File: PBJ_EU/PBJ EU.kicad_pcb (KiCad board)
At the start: 2 copper layers, 111.4 x 128.5 mm, 79 parts, among them J1 Molex_47257-spankulator-rescue, J2 Molex_47257-spankulator-rescue, J3 Molex_47257-spankulator-rescue, J4 Molex_47257-spankulator-rescue, J7 Conn_02x08_Odd_Even, J9 Conn_02x08_Odd_Even, SW1 SW_SPDT, SW2 SW_SPDT, U1 TL072, U2 TL072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

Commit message: ver 3.0
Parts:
- removed C10, C11, C8, C9: .1uF, Capacitor_THT:C_Rect_L7.0mm_W2.0mm_P5.00mm
- removed R25, R26: 91K, Resistor_THT:R_Axial_DIN0207_L6.3mm_D2.5mm_P10.16mm_Horizontal
- removed R28, R29, R5: 200K, Resistor_THT:R_Axial_DIN0207_L6.3mm_D2.5mm_P10.16mm_Horizontal
- removed U3, U4: TL072, Package_DIP:DIP-8_W7.62mm
- added D12: 1N4733A, Diode_THT:D_DO-41_SOD81_P10.16mm_Horizontal, F.Cu at (75.6, 131.0)
- added D14: 1N4733A, Diode_THT:D_DO-41_SOD81_P10.16mm_Horizontal, F.Cu at (104.5, 131.0)
- added D15: 1N4733A, Diode_THT:D_DO-41_SOD81_P10.16mm_Horizontal, F.Cu at (101.7, 131.0)
- added D16: 1N4733A, Diode_THT:D_DO-41_SOD81_P10.16mm_Horizontal, F.Cu at (143.9, 132.7)
- added D17: 1N4733A, Diode_THT:D_DO-41_SOD81_P10.16mm_Horizontal, F.Cu at (147.3, 129.1)
- added D3: 1N4733A, Diode_THT:D_DO-41_SOD81_P10.16mm_Horizontal, F.Cu at (49.7, 132.6)
- added D6: 1N4733A, Diode_THT:D_DO-41_SOD81_P10.16mm_Horizontal, F.Cu at (49.7, 129.3)
- added D9: 1N4733A, Diode_THT:D_DO-41_SOD81_P10.16mm_Horizontal, F.Cu at (78.5, 131.0)
- added R3: 470, Resistor_THT:R_Axial_DIN0207_L6.3mm_D2.5mm_P10.16mm_Horizontal, F.Cu at (104.7, 135.9)
- C4, C5, C6, C7, R10, R11, R16, R17, R34, R35, R40, R41, R43, U1, U2, U7: moved to B.Cu
- D1, D2, D7, D8: value LED -> RED LED
- D10, D11, D4, D5: value LED -> BLUE LED
- D13: value LED -> GREEN LED
- J9: value Conn_02x08_Odd_Even -> Conn_02x08_Odd_Even_Female
- R1, R2: value 91K -> 470
- R13, R14, R22, R23, R37, R38, R47, R48: value 100 -> 1K
- R4: value 200K -> 470
- moved R4 95.9 mm to (143.9, 135.9), turned to 180 degrees
- moved C7 66.5 mm to (126.4, 99.5), turned to 180 degrees
- moved C5 50.3 mm to (71.0, 99.6), turned to 180 degrees
- moved C6 45.9 mm to (126.5, 113.2)
- moved U2 42.8 mm to (120.2, 110.2)
- moved R40 36.0 mm to (74.3, 105.2), turned to 0 degrees
- moved R41 35.4 mm to (130.1, 105.2), turned to 0 degrees
- moved R16 28.0 mm to (62.2, 107.6), turned to 180 degrees
- moved R17 27.8 mm to (118.0, 107.7), turned to 180 degrees
- moved C4 27.1 mm to (70.8, 113.2)
- moved R34 24.1 mm to (84.5, 102.0), turned to 180 degrees
- moved R35 23.7 mm to (140.2, 102.1), turned to 180 degrees
- moved R10 22.8 mm to (52.1, 104.5), turned to 0 degrees
- moved R11 22.4 mm to (107.8, 104.6), turned to 0 degrees
- moved U1 20.7 mm to (64.5, 110.2)
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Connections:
- D1 pad 1: GND -> Net-(D1-Pad1)
- D1 pad 2: Net-(D1-Pad2) -> GND
- D2 pad 1: GND -> Net-(D2-Pad1)
- D2 pad 2: Net-(D2-Pad2) -> GND
- D7 pad 1: GND -> Net-(D7-Pad1)
- D7 pad 2: Net-(D7-Pad2) -> GND
- D8 pad 1: GND -> Net-(D8-Pad1)
- D8 pad 2: Net-(D8-Pad2) -> GND
- R1 pad 1: Net-(R1-Pad1) -> Tip1
- R1 pad 2: GND -> Net-(D3-Pad2)
- R10 pad 1: Tip1 -> Net-(D3-Pad2)
- R11 pad 1: Tip3 -> Net-(D14-Pad2)
- R13 pad 2: Net-(D1-Pad2) -> Net-(D1-Pad1)
- R14 pad 2: Net-(D2-Pad2) -> Net-(D2-Pad1)
- R16 pad 2: Net-(R16-Pad2) -> Net-(R13-Pad1)
- R17 pad 2: Net-(R17-Pad2) -> Net-(R14-Pad1)
- R2 pad 1: Net-(R2-Pad1) -> Tip2
- R2 pad 2: GND -> Net-(D9-Pad2)
- R22 pad 1: Net-(R16-Pad2) -> Net-(R13-Pad1)
- R23 pad 1: Net-(R17-Pad2) -> Net-(R14-Pad1)
- R31 pad 1: +12V -> Net-(D7-Pad1)
- R31 pad 2: Net-(D7-Pad2) -> -12V
- R32 pad 1: +12V -> Net-(D8-Pad1)
- R32 pad 2: Net-(D8-Pad2) -> -12V
- R34 pad 1: Tip2 -> Net-(D9-Pad2)
- R35 pad 1: Tip4 -> Net-(D16-Pad2)
- R37 pad 1: Net-(R28-Pad2) -> Net-(R37-Pad1)
- R37 pad 2: Net-(D7-Pad2) -> Net-(D7-Pad1)
- R38 pad 1: Net-(R29-Pad2) -> Net-(R38-Pad1)
- R38 pad 2: Net-(D8-Pad2) -> Net-(D8-Pad1)
- R4 pad 1: Net-(R1-Pad1) -> Tip4
- R4 pad 2: Net-(R13-Pad1) -> Net-(D16-Pad2)
- R40 pad 2: Net-(R40-Pad2) -> Net-(R37-Pad1)
- R41 pad 2: Net-(R41-Pad2) -> Net-(R38-Pad1)
- R47 pad 1: Net-(R40-Pad2) -> Net-(R37-Pad1)
- R48 pad 1: Net-(R41-Pad2) -> Net-(R38-Pad1)
- R7 pad 1: +12V -> Net-(D1-Pad1)
- R7 pad 2: Net-(D1-Pad2) -> -12V
- R8 pad 1: +12V -> Net-(D2-Pad1)
- R8 pad 2: Net-(D2-Pad2) -> -12V
- U1 pad 2: Net-(R1-Pad1) -> Net-(R10-Pad2)
- U1 pad 3: Tip1 -> GND
- U1 pad 6: Net-(R10-Pad2) -> Net-(R34-Pad2)
- U1 pad 7: Net-(R16-Pad2) -> Net-(R37-Pad1)
- U2 pad 1: Net-(R28-Pad2) -> Net-(R14-Pad1)
- U2 pad 2: Net-(R25-Pad1) -> Net-(R11-Pad2)
- U2 pad 3: Tip2 -> GND
- U2 pad 6: Net-(R34-Pad2) -> Net-(R35-Pad2)
- U2 pad 7: Net-(R40-Pad2) -> Net-(R38-Pad1)
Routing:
- net Net-(R38-Pad1): track 0.00 -> 75.9 mm, vias 0 -> 1
- net Net-(R37-Pad1): track 0.00 -> 63.3 mm
- net -12V: track 164.0 -> 222.3 mm, vias 6 -> 4
- net Net-(D3-Pad2): track 0.00 -> 45.8 mm, vias 0 -> 1
- net Net-(D16-Pad2): track 0.00 -> 44.3 mm, vias 0 -> 1
- net Net-(R13-Pad1): track 17.7 -> 61.9 mm
- net Net-(D9-Pad2): track 0.00 -> 43.5 mm, vias 0 -> 1
- net Net-(R14-Pad1): track 27.2 -> 70.2 mm, vias 0 -> 1
- net Net-(D14-Pad2): track 0.00 -> 38.6 mm
- net Net-(R29-Pad2): track 30.6 -> 0.00 mm, vias 2 -> 0
- net Net-(D2-Pad1): track 0.00 -> 26.4 mm, vias 0 -> 1
- net Net-(D1-Pad2): track 25.9 -> 0.00 mm
- net Net-(D2-Pad2): track 25.9 -> 0.00 mm, vias 1 -> 0
- net Net-(D7-Pad2): track 24.2 -> 0.00 mm
- net Tip3: track 79.4 -> 55.3 mm, vias 3 -> 1
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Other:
- board text added: "v3.0"
- board text removed: "v2.0"

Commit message: Fixed rescue libs
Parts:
- removed D12, D14, D15, D16, D17, D3, D6, D9: 1N4733A, Diode_THT:D_DO-41_SOD81_P10.16mm_Horizontal
- removed R1, R2, R3, R4: 470, Resistor_THT:R_Axial_DIN0207_L6.3mm_D2.5mm_P10.16mm_Horizontal
- added GR1: small_logo, panel:small_face, F.Cu at (128.6, 132.1)
- added J10: Conn_02x05_Odd_Even, Connector_PinHeader_2.54mm:PinHeader_2x05_P2.54mm_Vertical, F.Cu at (142.3, 133.8)
- added SW5: SW_DPST, sputterizer:S202031MS02Q, F.Cu at (67.0, 128.5)
- C1, C2, R13, R14, R37, R38: moved to B.Cu
- J7: value Conn_02x08_Odd_Even -> Conn_02x05_Odd_Even; footprint Connector_PinHeader_2.54mm:PinHeader_2x08_P2.54mm_Vertical -> Connector_PinHeader_2.54mm:PinHeader_2x05_P2.54mm_Vertical
- R10, R11, R34, R35: value 100K -> 1.00M
- R16, R17, R40, R41: value 330K -> 3.32M
- R19, R20, R31, R32, R44, R45, R7, R8: value 20K -> 10K; moved to B.Cu
- R22, R23, R47, R48: value 1K -> 2.2K; moved to B.Cu
- moved R43 105.7 mm to (42.9, 118.0), turned to 90 degrees
- moved D13 105.7 mm to (42.9, 123.0), turned to 0 degrees
- moved C2 46.8 mm to (102.5, 86.8)
- moved U7 46.8 mm to (92.9, 86.8)
- moved C1 46.8 mm to (83.7, 87.0)
- moved R14 41.7 mm to (117.8, 110.7), turned to 180 degrees
- moved R38 40.4 mm to (130.1, 107.7), turned to 0 degrees
- moved R13 33.5 mm to (62.2, 110.7), turned to 180 degrees
- moved R47 32.3 mm to (74.6, 110.8), turned to 0 degrees
- moved R48 31.7 mm to (130.1, 110.8), turned to 0 degrees
- moved R7 30.9 mm to (52.1, 113.9), turned to 0 degrees
- moved R37 30.2 mm to (74.6, 107.7), turned to 0 degrees
- moved R44 27.8 mm to (76.8, 117.1), turned to 0 degrees
- moved R45 27.1 mm to (132.4, 116.9), turned to 0 degrees
- moved R32 24.6 mm to (140.3, 113.9)
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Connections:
- J7 pad 1: -12V -> Net-(J7-Pad1)
- J7 pad 10: +12V -> Net-(J7-Pad10)
- J7 pad 2: -12V -> Net-(J7-Pad1)
- J7 pad 9: +12V -> Net-(J7-Pad10)
- R10 pad 1: Net-(D3-Pad2) -> Tip1
- R11 pad 1: Net-(D14-Pad2) -> Tip3
- R34 pad 1: Net-(D9-Pad2) -> Tip2
- R35 pad 1: Net-(D16-Pad2) -> Tip4
- SW1 pad 1: Net-(SW1-Pad1) -> Tip1
- SW1 pad 3: Tip1 -> Net-(SW1-Pad3)
- SW2 pad 1: Net-(SW2-Pad1) -> Tip3
- SW2 pad 3: Tip3 -> Net-(SW2-Pad3)
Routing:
- net +5V: track 49.5 -> 142.3 mm
- net Net-(R38-Pad1): track 75.9 -> 18.6 mm, vias 1 -> 0
- net -12V: track 222.3 -> 169.3 mm, vias 4 -> 7
- net Net-(R14-Pad1): track 70.2 -> 24.3 mm, vias 1 -> 0
- net Net-(D3-Pad2): track 45.8 -> 0.00 mm, vias 1 -> 0
- net Net-(R37-Pad1): track 63.3 -> 18.4 mm
- net Net-(D16-Pad2): track 44.3 -> 0.00 mm, vias 1 -> 0
- net Net-(D9-Pad2): track 43.5 -> 0.00 mm, vias 1 -> 0
- net Net-(D14-Pad2): track 38.6 -> 0.00 mm
- net Net-(R13-Pad1): track 61.9 -> 24.3 mm
- net Net-(D11-Pad2): track 7.01 -> 41.0 mm
- net Net-(D10-Pad2): track 7.51 -> 40.0 mm
- net Net-(J7-Pad10): track 0.00 -> 31.7 mm
- net Tip3: track 55.3 -> 86.9 mm, vias 1 -> 4
- net Net-(J7-Pad1): track 0.00 -> 30.7 mm
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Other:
- board text added: "EU Power Out"
- board text added: "Mult 1&2"
- board text added: "Mult 3&4"
- board text added: "ON"
- board text added: "v4.0"
- board text removed: "v3.0"

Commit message: Updates to ver 4.7.
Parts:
- added R1: 750K, Resistor_THT:R_Axial_DIN0207_L6.3mm_D2.5mm_P10.16mm_Horizontal, B.Cu at (62.2, 98.0)
- added R2: 750K, Resistor_THT:R_Axial_DIN0207_L6.3mm_D2.5mm_P10.16mm_Horizontal, B.Cu at (117.9, 98.0)
- added R3: 750K, Resistor_THT:R_Axial_DIN0207_L6.3mm_D2.5mm_P10.16mm_Horizontal, B.Cu at (62.2, 101.3)
- added R4: 750K, Resistor_THT:R_Axial_DIN0207_L6.3mm_D2.5mm_P10.16mm_Horizontal, B.Cu at (117.8, 101.3)
- J1, J2, J3, J4: value Molex_47257-spankulator-rescue -> Molex_47257
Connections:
- U1 pad 3: GND -> Net-(R1-Pad1)
- U1 pad 5: GND -> Net-(R3-Pad1)
- U2 pad 3: GND -> Net-(R2-Pad1)
- U2 pad 5: GND -> Net-(R4-Pad1)
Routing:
- net Net-(R4-Pad1): track 0.00 -> 10.6 mm
- net Net-(R3-Pad1): track 0.00 -> 10.4 mm
- net Net-(R2-Pad1): track 0.00 -> 8.05 mm
- net Net-(R1-Pad1): track 0.00 -> 8.02 mm
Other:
- board text added: "v4.7"
- board text removed: "v4.0"

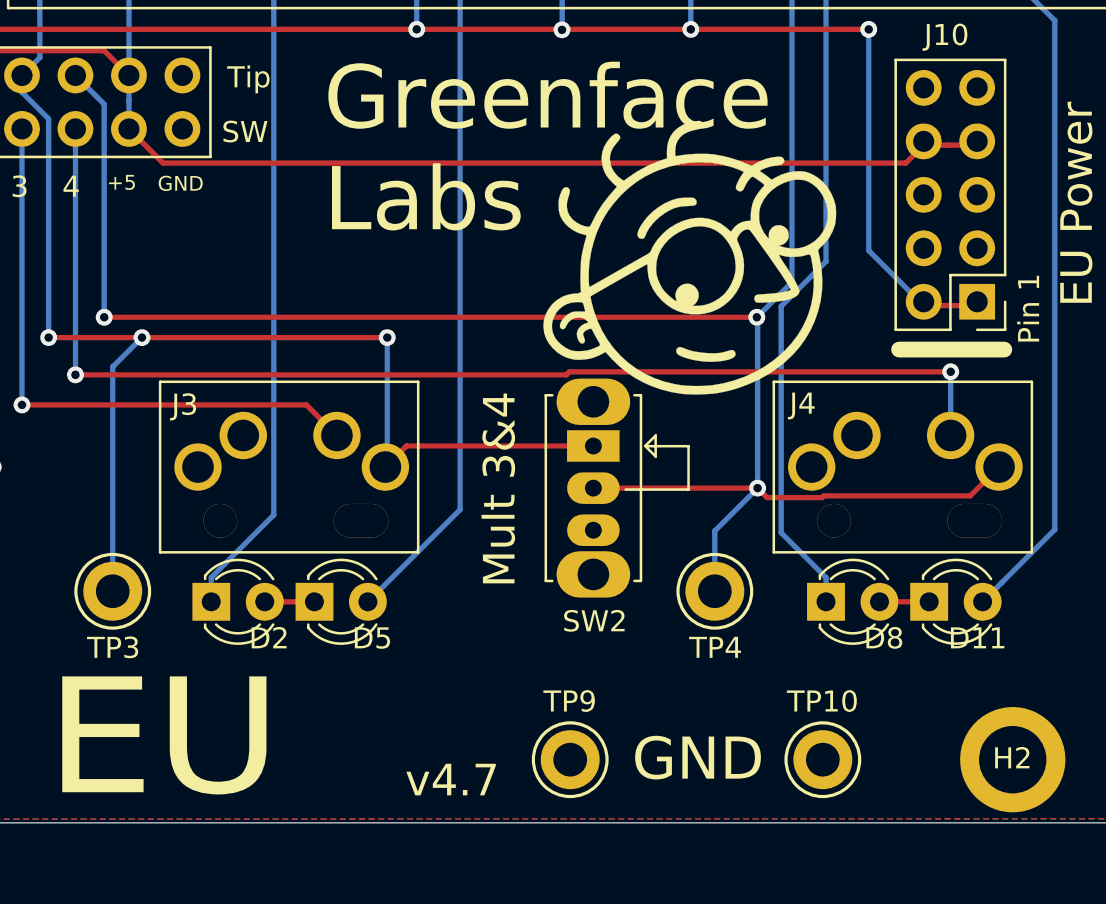
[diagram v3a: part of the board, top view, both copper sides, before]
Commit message: version 4.8
Fixes power connector.
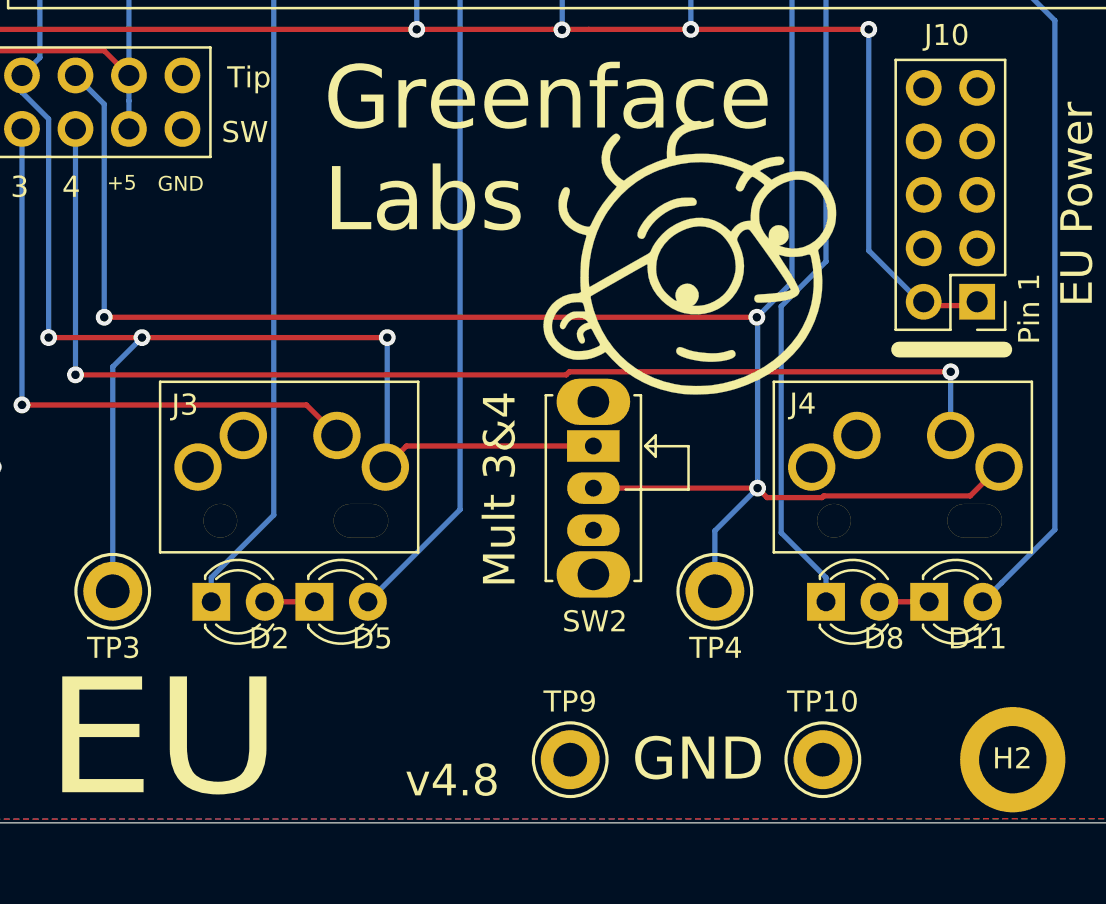
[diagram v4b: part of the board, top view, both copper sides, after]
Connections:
- J1 pad 3: Net-(J1-Pad3) -> (no net)
- J10 pad 7: +5V -> GND
- J10 pad 8: +5V -> GND
- J2 pad 3: Net-(J2-Pad3) -> (no net)
- J3 pad 3: Net-(J3-Pad3) -> (no net)
- J4 pad 3: Net-(J4-Pad3) -> (no net)
- J7 pad 7: Net-(J7-Pad7) -> GND
- J7 pad 8: Net-(J7-Pad8) -> GND
- SW1 pad 3: Net-(SW1-Pad3) -> (no net)
- SW2 pad 3: Net-(SW2-Pad3) -> (no net)
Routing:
- net +5V: track 142.3 -> 101.0 mm
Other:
- board text added: "v4.8"
- board text removed: "v4.7"

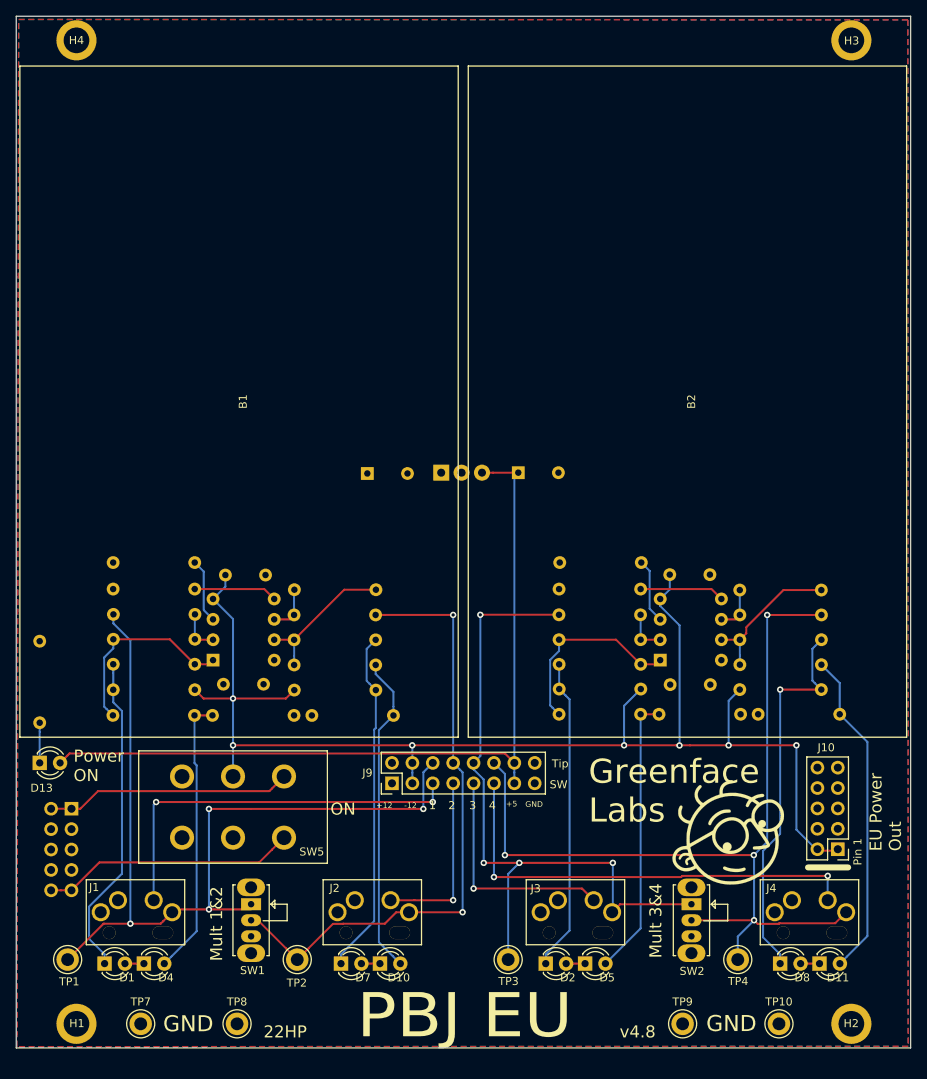
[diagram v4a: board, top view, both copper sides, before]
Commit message: v 4.9
Adds caps to regulator. Adds graphics and text.
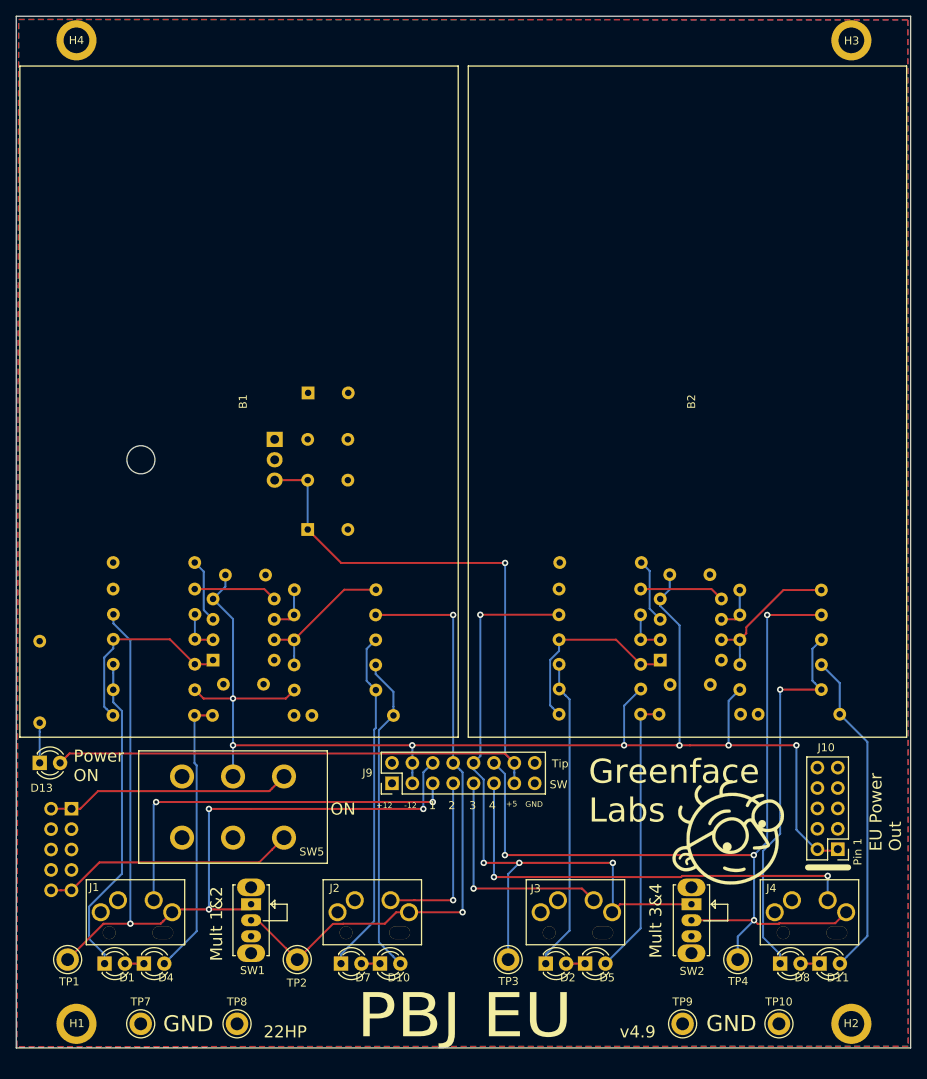
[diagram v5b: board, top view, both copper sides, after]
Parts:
- added C3: .33uF, Capacitor_THT:C_Rect_L7.0mm_W2.0mm_P5.00mm, B.Cu at (76.3, 82.7)
- added C8: .1uF, Capacitor_THT:C_Rect_L7.0mm_W2.0mm_P5.00mm, B.Cu at (76.3, 87.8)
- added GR2: big_logo, panel:logo_black, B.Cu at (121.5, 59.9)
- U7: footprint digikey-footprints:TO-220-3 -> Package_TO_SOT_THT:TO-220-3_Horizontal_TabDown
- moved C2 27.2 mm to (76.3, 93.9)
- moved U7 21.2 mm to (72.2, 82.7), turned to 270 degrees
- moved C1 12.5 mm to (76.4, 76.9)
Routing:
- net +5V: track 101.0 -> 122.0 mm, vias 0 -> 1
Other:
- board text added: "Eurorack Synthesizer Prototyping System"
- board text added: "Note inverted orientation of U1 & U2"
- board text added: "SN"
- board text added: "v4.9"
- board text removed: "v4.8"

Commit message: Move to KiCAD 6.0
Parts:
- U7: footprint Package_TO_SOT_THT:TO-220-3_Horizontal_TabDown -> Package_TO_SOT_THT:TO-220-3_Vertical
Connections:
- J1 pad 3: (no net) -> unconnected-(J1-Pad3)
- J2 pad 3: (no net) -> unconnected-(J2-Pad3)
- J3 pad 3: (no net) -> unconnected-(J3-Pad3)
- J4 pad 3: (no net) -> unconnected-(J4-Pad3)
- SW1 pad 3: (no net) -> unconnected-(SW1-Pad3)
- SW2 pad 3: (no net) -> unconnected-(SW2-Pad3)
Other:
- net class Default removed
